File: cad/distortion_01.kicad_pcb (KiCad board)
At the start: 2 copper layers, 179 x 110 mm, 100 parts, among them CON101 Ext_PSU, J101 JACK_IN, J102 JACK_OUT, P101 Battery_conn, P102 BYPASS_SWITCH, P103 CONN_01X03, P104 CONN_01X03, P105 CONN_01X03, P106 CONN_01X03, Q101 BS170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

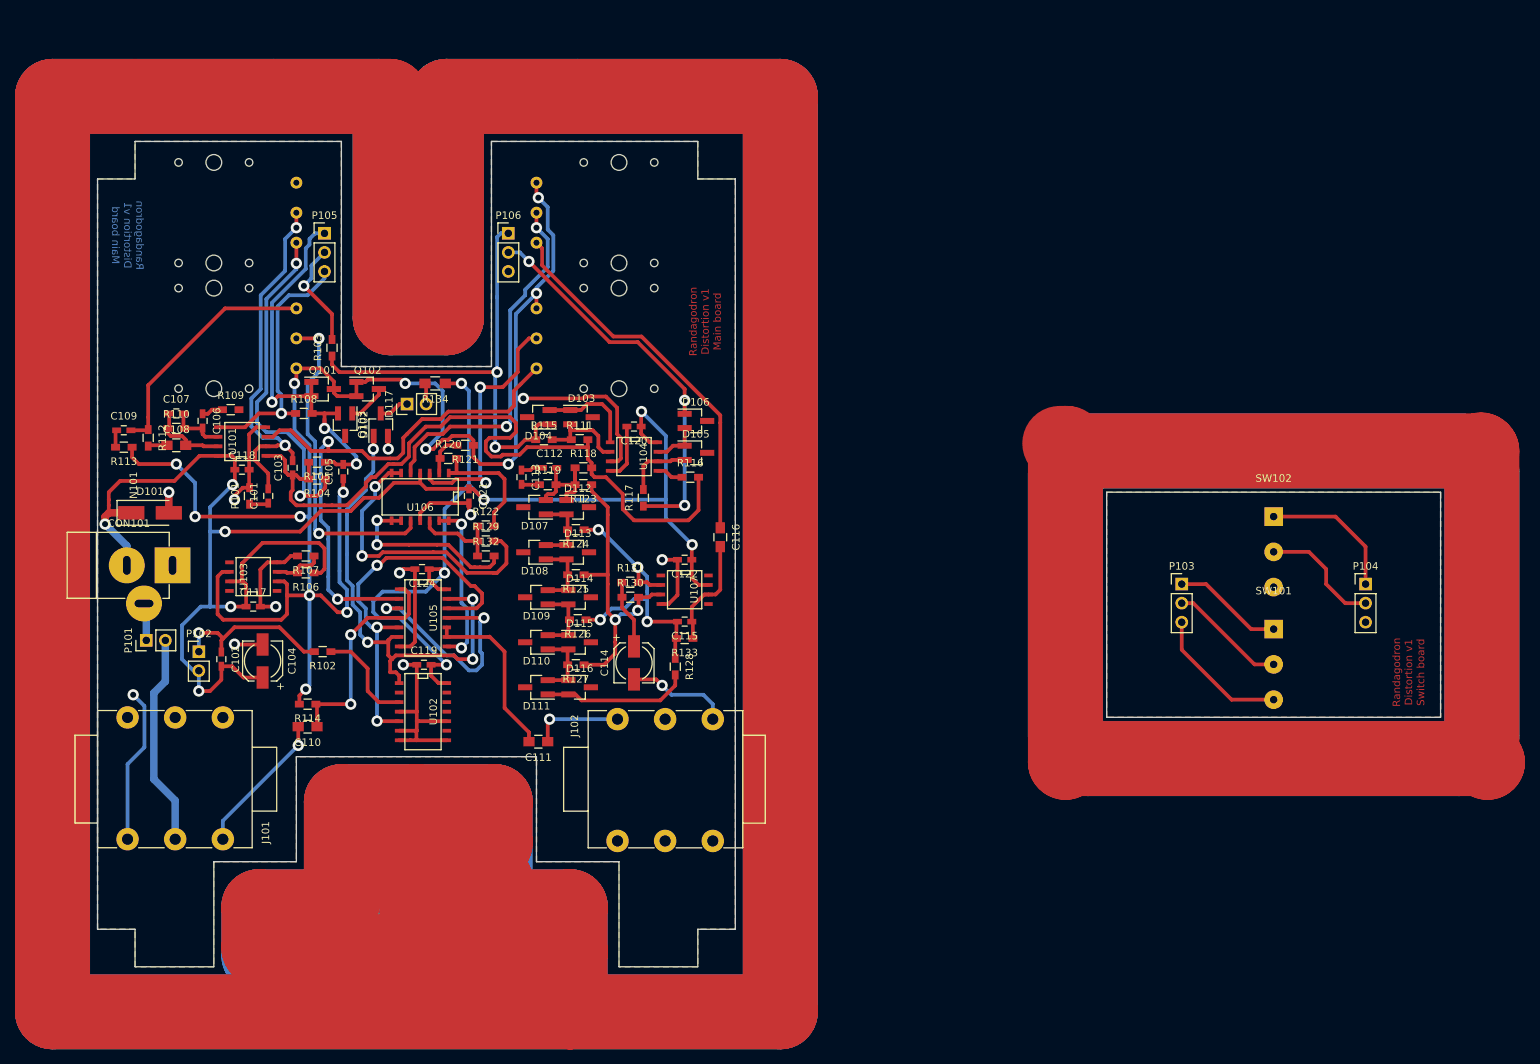
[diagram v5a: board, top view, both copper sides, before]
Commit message: Started placement. Output OPA TL074 changed to 2x TL072.
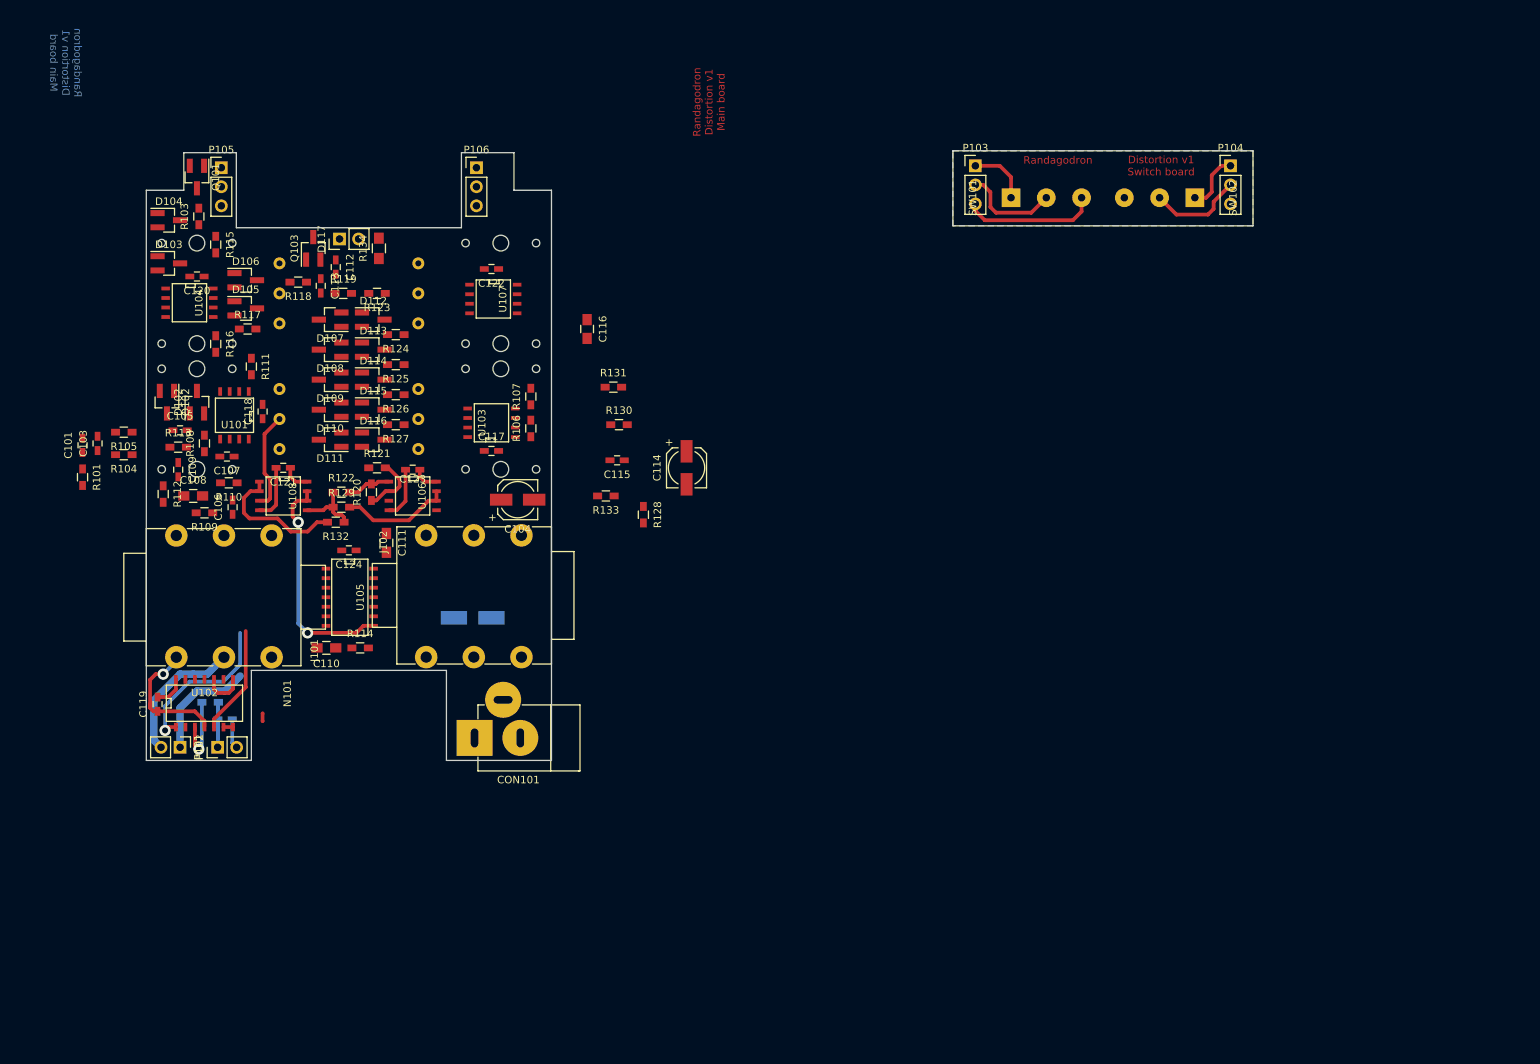
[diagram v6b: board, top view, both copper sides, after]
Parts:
- added C123: 100n, Capacitors_SMD:C_0603_HandSoldering, F.Cu at (76.0, 75.8)
- added U108: TL072, SMD_Packages:SOIC-8-N, F.Cu at (58.8, 79.2)
- C102, D101, R102: moved to B.Cu
- U106: value TL074 -> TL072; footprint SMD_Packages:SOIC-14_N -> SMD_Packages:SOIC-8-N
- moved SW101 67.3 mm to (155.8, 39.5), turned to 90 degrees
- moved R116 65.7 mm to (49.8, 59.0), turned to 270 degrees
- moved D105 63.0 mm to (53.8, 54.2)
- moved D106 62.9 mm to (53.8, 50.5)
- moved U104 62.7 mm to (46.2, 53.5)
- moved P103 62.2 mm to (151.0, 35.2)
- moved C120 61.6 mm to (47.2, 50.0)
- moved D103 58.7 mm to (43.5, 48.2)
- moved P104 58.6 mm to (185.0, 35.2)
- moved R117 57.3 mm to (54.0, 57.0), turned to 0 degrees
- moved D104 55.8 mm to (43.5, 42.5), turned to 0 degrees
- moved R115 50.9 mm to (49.8, 45.8), turned to 270 degrees
- moved C122 46.5 mm to (86.5, 49.0)
- moved U107 46.4 mm to (86.8, 53.0)
- moved CON101 46.4 mm to (84.2, 111.5), turned to 180 degrees
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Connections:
- U106 pad 4: +9V -> GND
- U106 pad 8: Net-(R132-Pad2) -> +9V
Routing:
- net (no net): track 1699.0 -> 0.00 mm
- net +9V: track 266.5 -> 15.3 mm, vias 10 -> 0
- net VCOM: track 240.2 -> 0.00 mm, vias 14 -> 0
- net GND: track 140.2 -> 38.8 mm, vias 11 -> 1
- net /audio_gain: track 100.1 -> 0.00 mm
- net /audio_fx_in: track 77.1 -> 0.00 mm, vias 2 -> 0
- net /audio_octave_out: track 63.6 -> 0.00 mm, vias 2 -> 0
- net Net-(D106-Pad1): track 53.9 -> 0.00 mm, vias 3 -> 0
- net Net-(C105-Pad2): track 53.8 -> 0.00 mm, vias 3 -> 0
- net Net-(C116-Pad1): track 50.3 -> 0.00 mm
- net Net-(C101-Pad2): track 49.1 -> 0.00 mm, vias 2 -> 0
- net /audio_prunes_out: track 48.5 -> 0.00 mm, vias 2 -> 0
- net Net-(R104-Pad1): track 45.3 -> 0.00 mm, vias 2 -> 0
- net /bypass_cmd: track 64.3 -> 21.4 mm, vias 4 -> 1
- net Net-(C115-Pad2): track 40.5 -> 0.00 mm, vias 4 -> 0
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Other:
- board size 179 x 110 mm -> 147.5 x 81.2 mm
- board text added: "Distortion v1 Switch board"
- board text added: "Randagodron"
- board text removed: "Randagodron Distortion v1 Switch board"

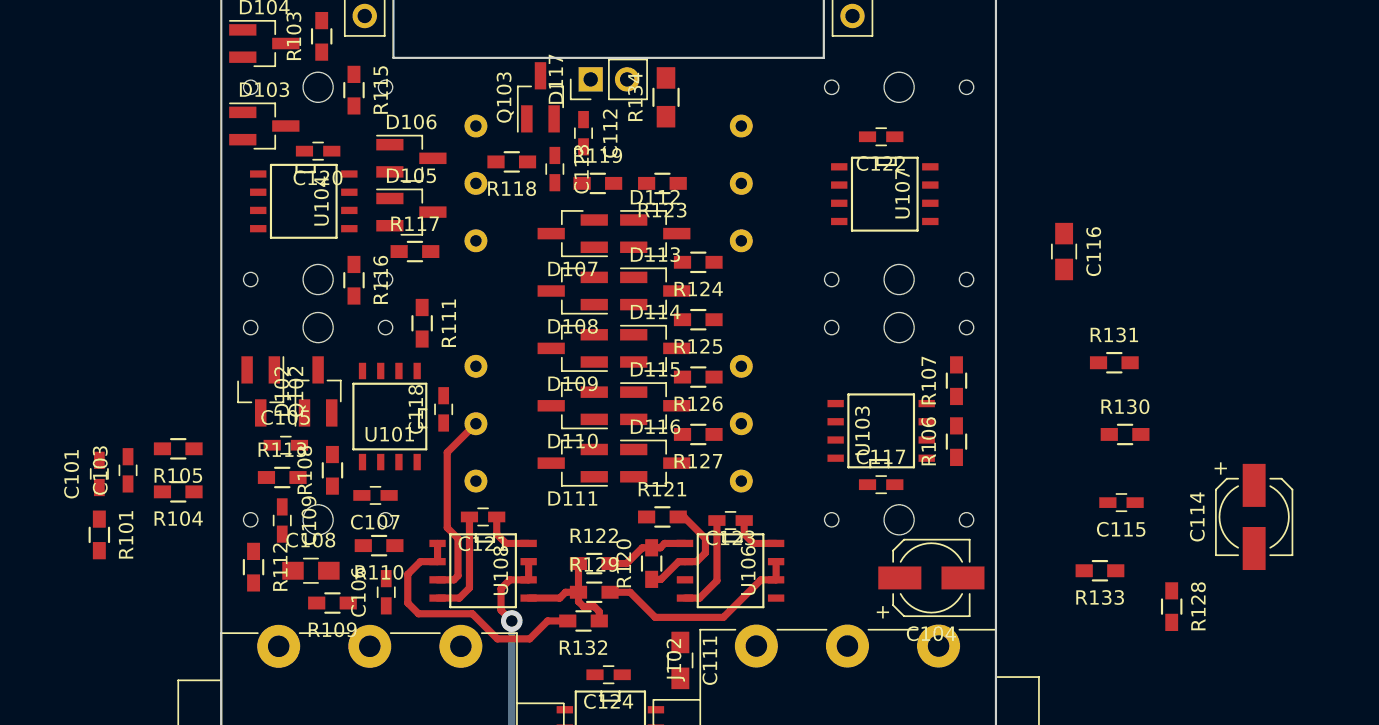
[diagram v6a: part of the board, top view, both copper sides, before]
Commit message: Added 220p capa in feedback loop of dry OPA. Placed all components on PCB.
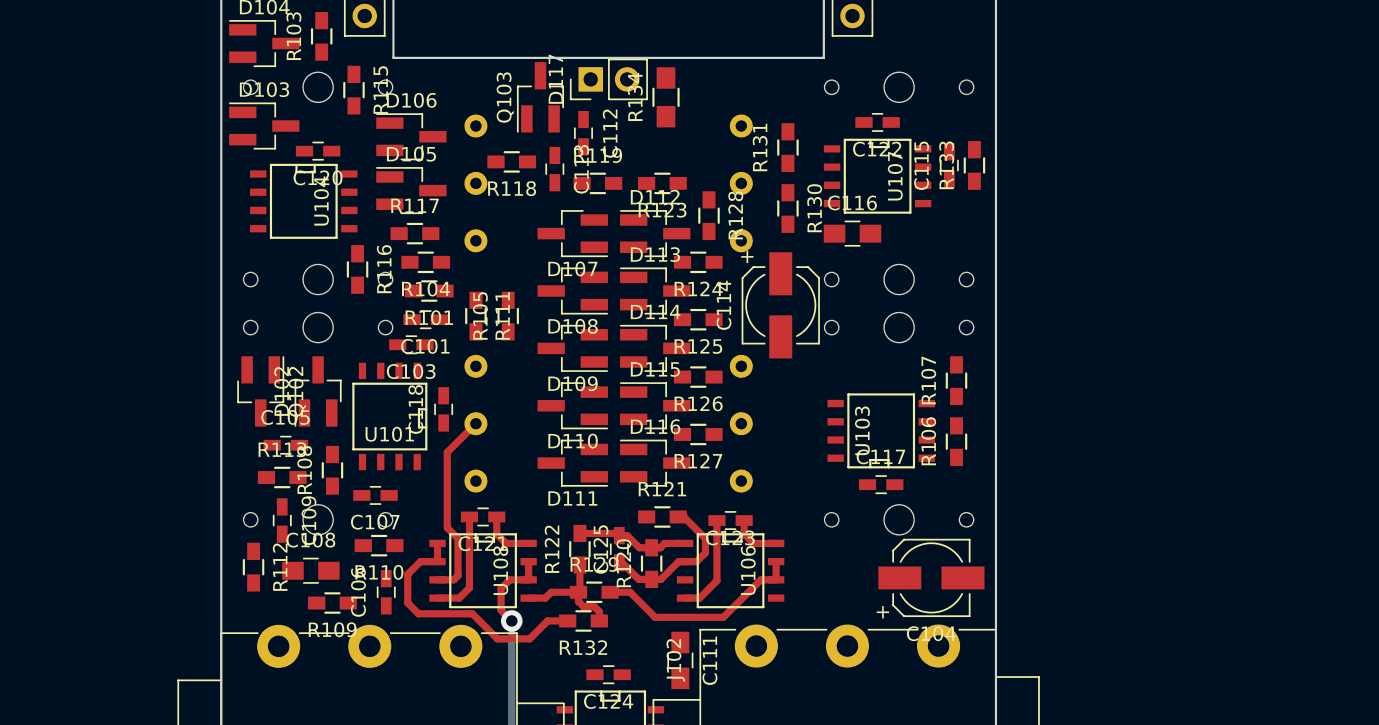
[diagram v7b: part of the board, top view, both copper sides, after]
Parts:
- added C125: 220p, Capacitors_SMD:C_0603_HandSoldering, F.Cu at (68.2, 77.8)
- moved R128 42.2 mm to (74.5, 54.5)
- moved C114 36.1 mm to (79.5, 60.8)
- moved R133 29.6 mm to (93.0, 51.0), turned to 90 degrees
- moved R101 28.6 mm to (55.0, 59.8), turned to 180 degrees
- moved R130 28.3 mm to (80.0, 54.0), turned to 270 degrees
- moved R131 27.2 mm to (80.0, 49.8), turned to 90 degrees
- moved C115 26.4 mm to (91.2, 51.0), turned to 90 degrees
- moved C101 25.2 mm to (54.8, 61.8), turned to 180 degrees
- moved R105 24.8 mm to (60.5, 61.5), turned to 90 degrees
- moved R104 23.5 mm to (54.8, 57.8)
- moved C103 21.6 mm to (53.8, 63.5), turned to 180 degrees
- moved C116 14.8 mm to (84.5, 55.8), turned to 0 degrees
- moved R111 3.78 mm to (58.2, 61.5)
- moved D105 1.50 mm to (53.8, 52.8)
- moved D106 1.50 mm to (53.8, 49.0)
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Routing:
- net Net-(C125-Pad1): track 8.04 -> 10.8 mm
- net Net-(C125-Pad2): track 5.81 -> 7.87 mm

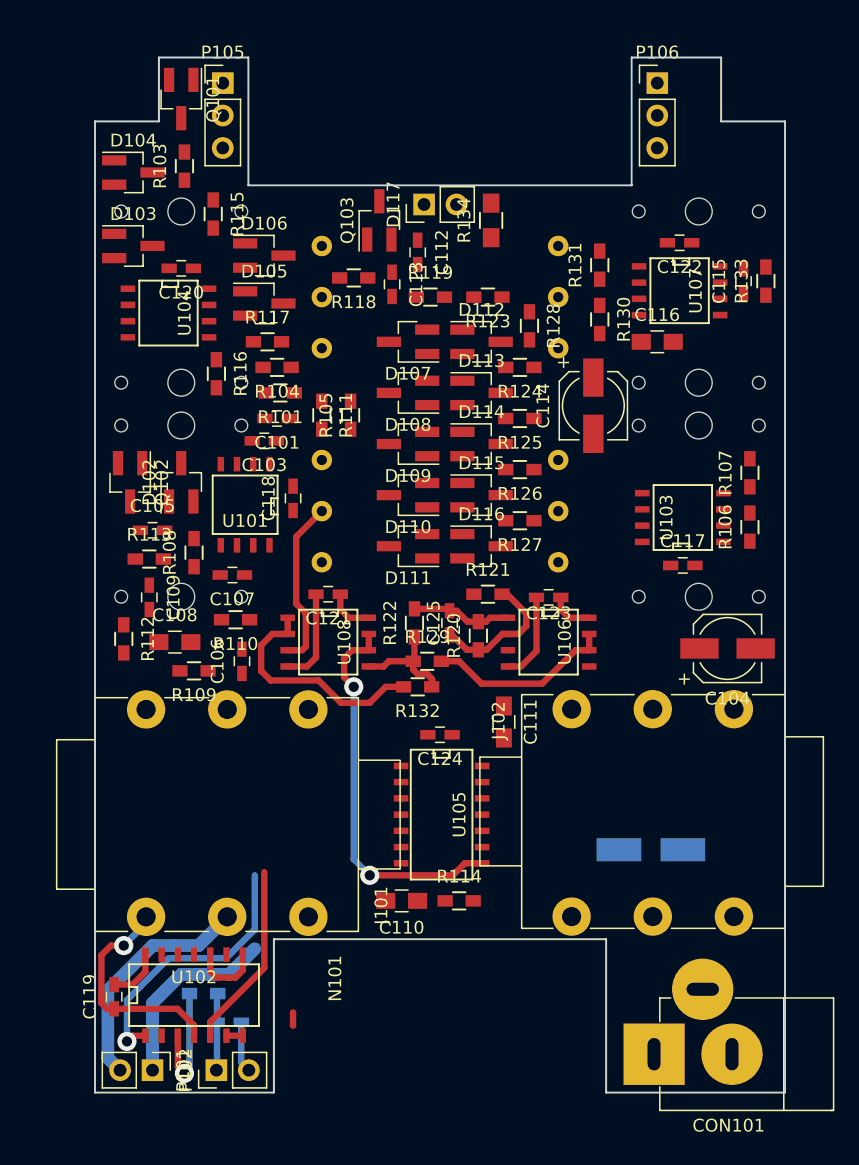
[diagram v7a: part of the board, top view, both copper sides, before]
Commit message: Continued layout. Changed 4066 pinout.
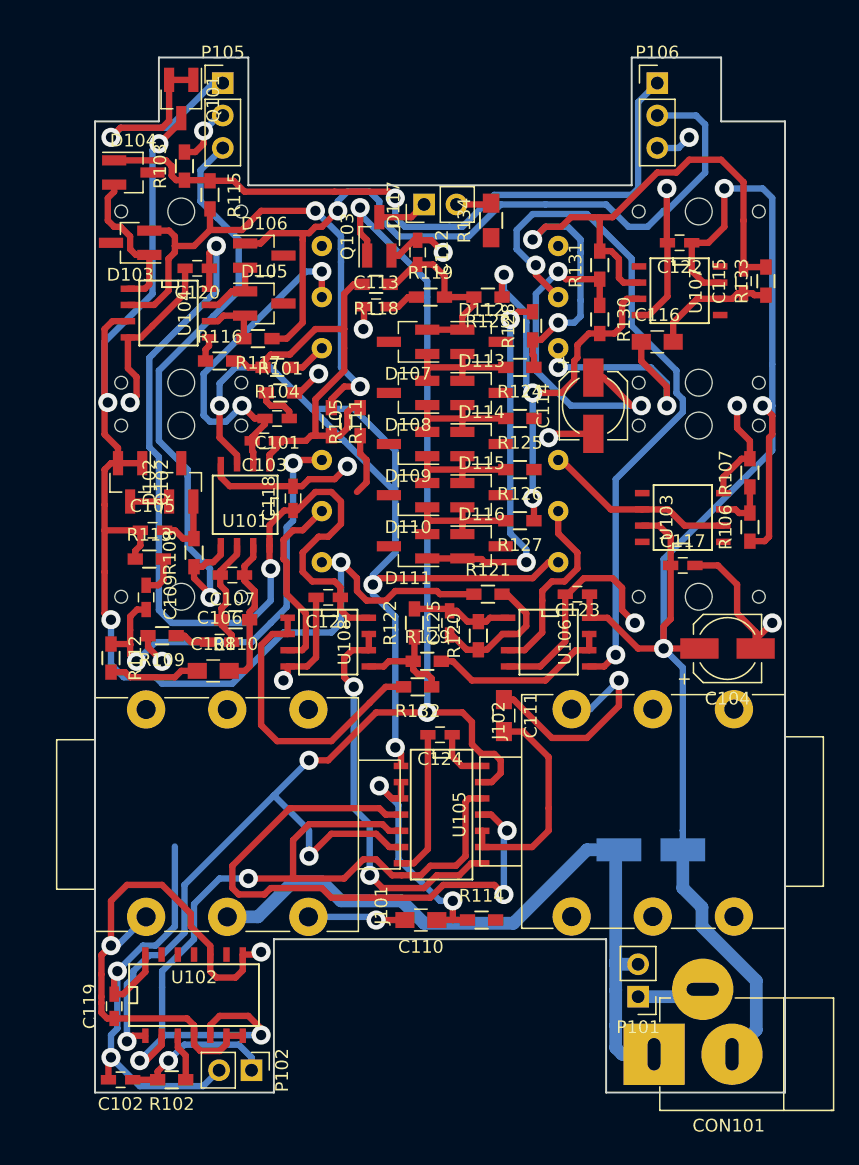
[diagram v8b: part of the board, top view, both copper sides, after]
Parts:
- C102, R102: moved to F.Cu
- N101: moved to B.Cu
- moved P101 38.4 mm to (83.0, 107.0), turned to 180 degrees
- moved N101 33.7 mm to (86.5, 94.5)
- moved C102 9.62 mm to (42.5, 113.5), turned to 180 degrees
- moved R102 7.20 mm to (46.5, 113.5), turned to 180 degrees
- moved C108 3.75 mm to (49.8, 81.5)
- moved R109 3.72 mm to (45.8, 78.8)
- moved P102 2.75 mm to (52.8, 112.8), turned to 270 degrees
- moved C106 2.30 mm to (50.2, 79.2), turned to 0 degrees
- moved R114 2.30 mm to (70.8, 101.0)
- moved C123 2.26 mm to (78.2, 75.5)
- moved C113 2.15 mm to (62.5, 53.0), turned to 0 degrees
- moved C110 2.12 mm to (66.0, 101.0)
- moved R118 1.82 mm to (62.5, 51.2)
- moved R112 1.80 mm to (41.8, 80.5)
- moved R115 1.52 mm to (49.5, 44.2)
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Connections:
- CON101 pad 1: GND -> GNDPWR
- D101 pad 2: GND -> GNDPWR
- U105 pad 1: /audio_jack_in -> /audio_fx_in
- U105 pad 2: /audio_fx_in -> /audio_jack_in
- U105 pad 3: /audio_bypass -> /audio_jack_in
- U105 pad 4: /audio_jack_in -> /audio_bypass
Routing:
- net +9V: track 15.3 -> 219.3 mm, vias 0 -> 7
- net GND: track 38.8 -> 162.3 mm, vias 1 -> 15
- net VCOM: track 0.00 -> 116.5 mm, vias 0 -> 4
- net /bypass_cmd: track 21.4 -> 111.9 mm, vias 1 -> 5
- net /audio_fx_in: track 0.00 -> 74.6 mm, vias 0 -> 3
- net Net-(D106-Pad1): track 0.00 -> 62.7 mm, vias 0 -> 1
- net /~bypass_cmd~: track 14.6 -> 72.7 mm, vias 0 -> 3
- net /audio_prunes_out: track 0.00 -> 55.5 mm, vias 0 -> 2
- net Net-(C115-Pad2): track 0.00 -> 55.3 mm, vias 0 -> 2
- net /audio_octave_out: track 0.00 -> 54.6 mm, vias 0 -> 1
- net Net-(P105-Pad3): track 0.00 -> 47.5 mm, vias 0 -> 1
- net /audio_bypass: track 0.00 -> 47.3 mm, vias 0 -> 2
- net Net-(D103-Pad2): track 0.00 -> 43.3 mm, vias 0 -> 2
- net GNDPWR: track 18.4 -> 57.8 mm
- net Net-(R123-Pad1): track 0.00 -> 35.9 mm, vias 0 -> 3
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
